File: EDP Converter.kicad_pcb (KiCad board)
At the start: 4 copper layers, 55.8 x 58.4 mm, 64 parts, among them J1 47272-0001, J2 Conn_01x22_Socket, J3 Conn_02x20_Odd_Even, U1 SN65DSI86IPAPRQ1, U2 MCP1700x-180xxTT, U3 MCP1700x-120xxTT, U4 TXB0104RGY, U5 74LVC1G07

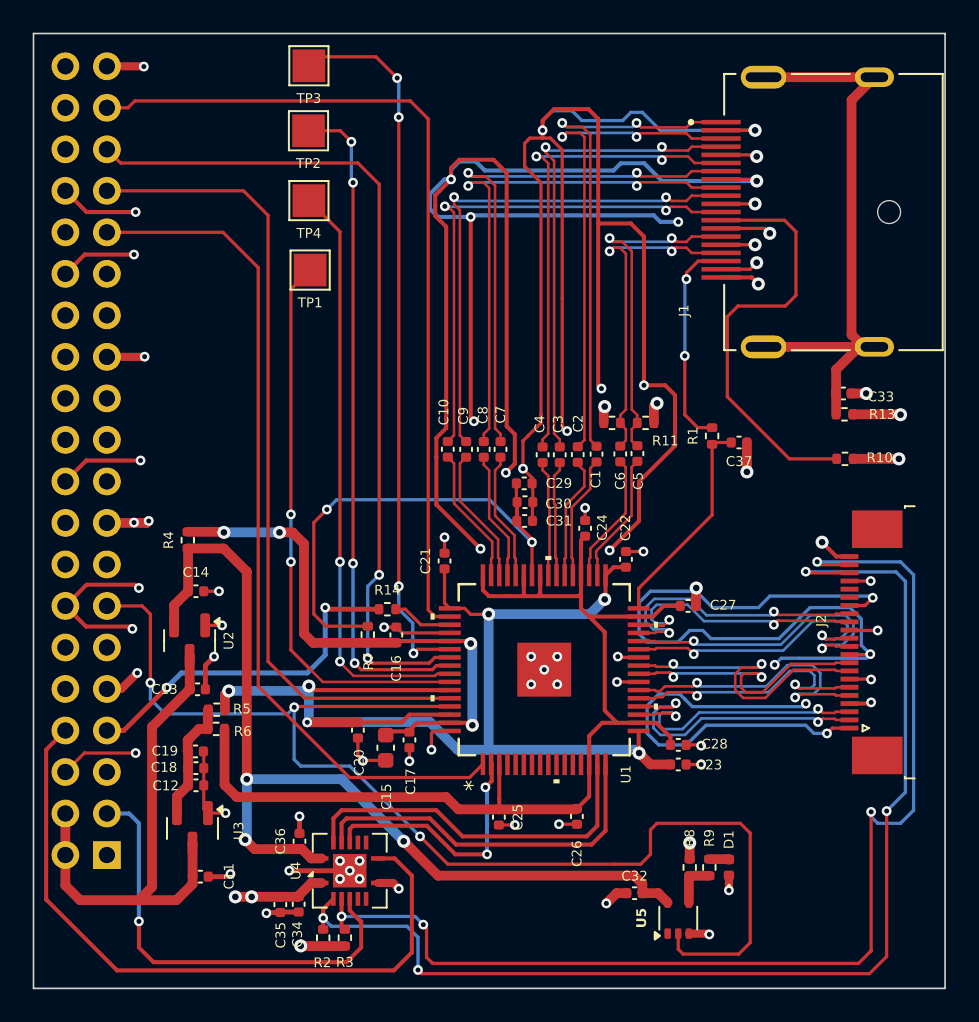
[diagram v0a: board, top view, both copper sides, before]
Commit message: added the v1.1 which few modifications
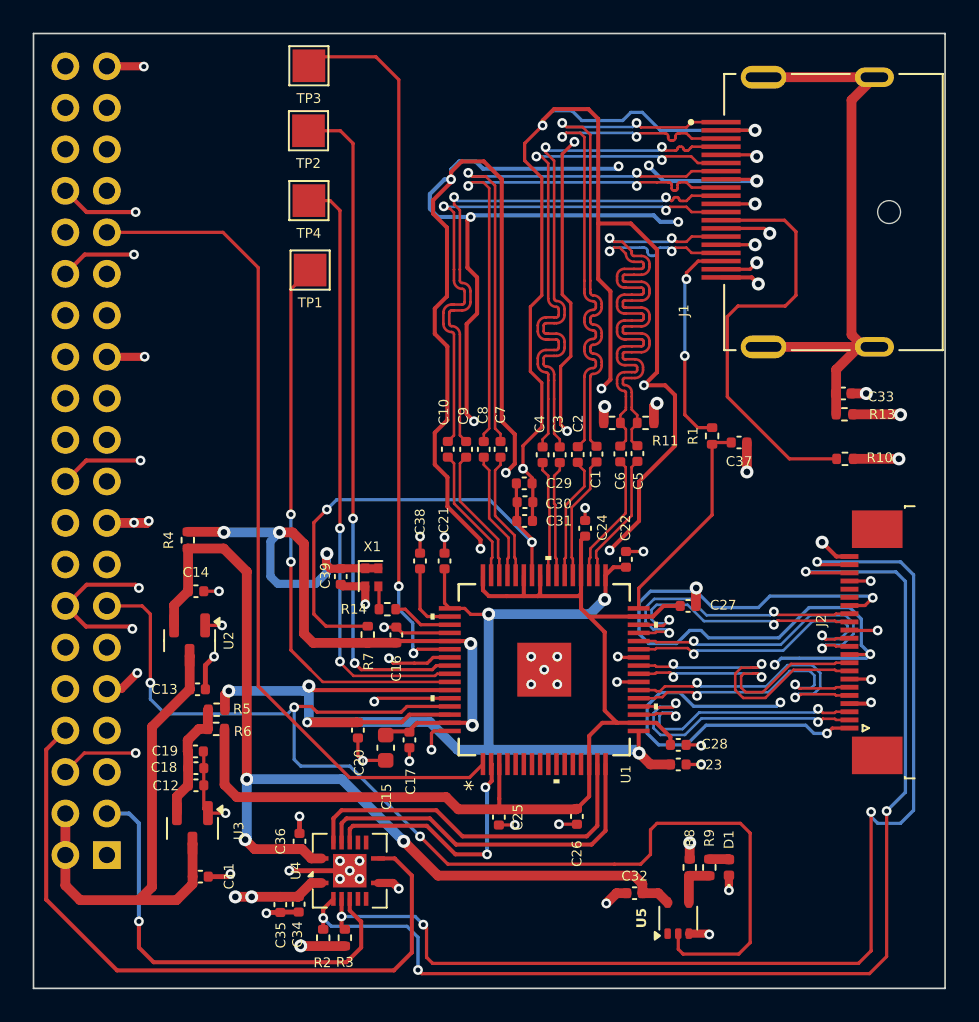
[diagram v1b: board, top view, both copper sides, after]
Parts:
- added C38: 100nF, Capacitor_SMD:C_0402_1005Metric, F.Cu at (118.6, 107.7)
- added C39: 100nF, Capacitor_SMD:C_0402_1005Metric, F.Cu at (113.8, 108.6)
- added X1: ASCO, Oscillator:Oscillator_SMD_Abracon_ASCO-4Pin_1.6x1.2mm, F.Cu at (115.7, 108.7)
- C16, C17, C18, C19, C21, C23, C25, C27, C30, C32, C34, C36: value 0.1uF -> 100nF
- C37: value 10nF -> 0.01uF
- R9: value 350 -> 348
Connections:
- J3 pad 33: /TEST_1 -> unconnected-(J3-Pin_33-Pad33)
- J3 pad 35: /TEST_2 -> unconnected-(J3-Pin_35-Pad35)
- J3 pad 37: /TEST_3 -> unconnected-(J3-Pin_37-Pad37)
- J3 pad 7: /REFCLK -> unconnected-(J3-Pin_7-Pad7)
- U1 pad 50: /TEST_3 -> Net-(U1-TEST3)
- U1 pad 55: /TEST_2 -> GND
- U1 pad 60: /TEST_1 -> GND
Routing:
- net /TEST_2: track 52.1 -> 0.00 mm, vias 2 -> 0
- net /TEST_3: track 51.8 -> 0.00 mm
- net /TEST_1: track 49.8 -> 0.00 mm
- net /REFCLK: track 21.5 -> 1.42 mm, vias 2 -> 0
- net /AUX_N: track 20.4 -> 33.5 mm
- net /AUX_P: track 21.0 -> 33.5 mm
- net VCCIO: track 34.1 -> 46.0 mm, vias 4 -> 5
- net GND: track 386.0 -> 396.5 mm, vias 78 -> 85
- net Net-(U1-TEST3): track 0.00 -> 4.48 mm
- net /ML1_P: track 29.8 -> 33.7 mm
- net /ML1_N: track 30.1 -> 33.7 mm
- net /ML0_N: track 30.8 -> 33.7 mm
- net /ML0_P: track 31.4 -> 33.6 mm
- net /ML3_P: track 31.8 -> 33.7 mm
- net /ML3_N: track 31.9 -> 33.8 mm
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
